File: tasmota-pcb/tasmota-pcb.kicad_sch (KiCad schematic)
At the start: 0 parts

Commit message: Add esp32 doit from https://gitlab.com/VictorLamoine/kicad
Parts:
- added U1: ESP32_DevKit_V1_DOIT, Doit:esp32_devkit_v1_doit, symbol Doit:ESP32_DevKit_V1_DOIT
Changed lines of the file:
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@@
 (kicad_sch (version 20230121) (generator eeschema)
   (paper "A4")
+  (symbol (lib_id "Doit:ESP32_DevKit_V1_DOIT") (at 124.46 91.44 0) (unit 1)
+    (in_bom yes) (on_board yes) (dnp no) (fields_autoplaced)
+    (property "Reference" "U1" (at 126.6541 53.34 0)
+      (effects (font (size 1.27 1.27)) (justify left))
+    )
+    (property "Value" "ESP32_DevKit_V1_DOIT" (at 126.6541 55.88 0)
+      (effects (font (size 1.27 1.27)) (justify left))
+    )
+    (property "Footprint" "Doit:esp32_devkit_v1_doit" (at 113.03 57.15 0)
+      (effects (font (size 1.27 1.27)) hide)
+    )
+    (property "Datasheet" "https://aliexpress.com/item/32864722159.html" (at 113.03 57.15 0)
+      (effects (font (size 1.27 1.27)) hide)
+    )
+    (pin "27")
+    (pin "30")
+    (pin "26")
+    (pin "22")
+    (pin "5")
+    (pin "15")
+    (pin "10")
+    (pin "16")
+    (pin "14")
+    (pin "6")
+    (pin "18")
+    (pin "21")
+    (pin "17")
+    (pin "19")
+    (pin "23")
+    (pin "28")
+    (pin "25")
+    (pin "4")
+    (pin "13")
+    (pin "3")
+    (pin "2")
+    (pin "20")
+    (pin "12")
+    (pin "11")
+    (pin "1")
+    (pin "24")
+    (pin "7")
+    (pin "9")
+    (pin "8")
+    (pin "29")
+    (instances
+      (project "tasmota-pcb"
+        (path "/0446fa3c-fa52-4d7b-8ba0-a6da357efbc3"
+          (reference "U1") (unit 1)
+        )
+      )
+    )
+  )
   (sheet_instances
     (path "/" (page "1"))

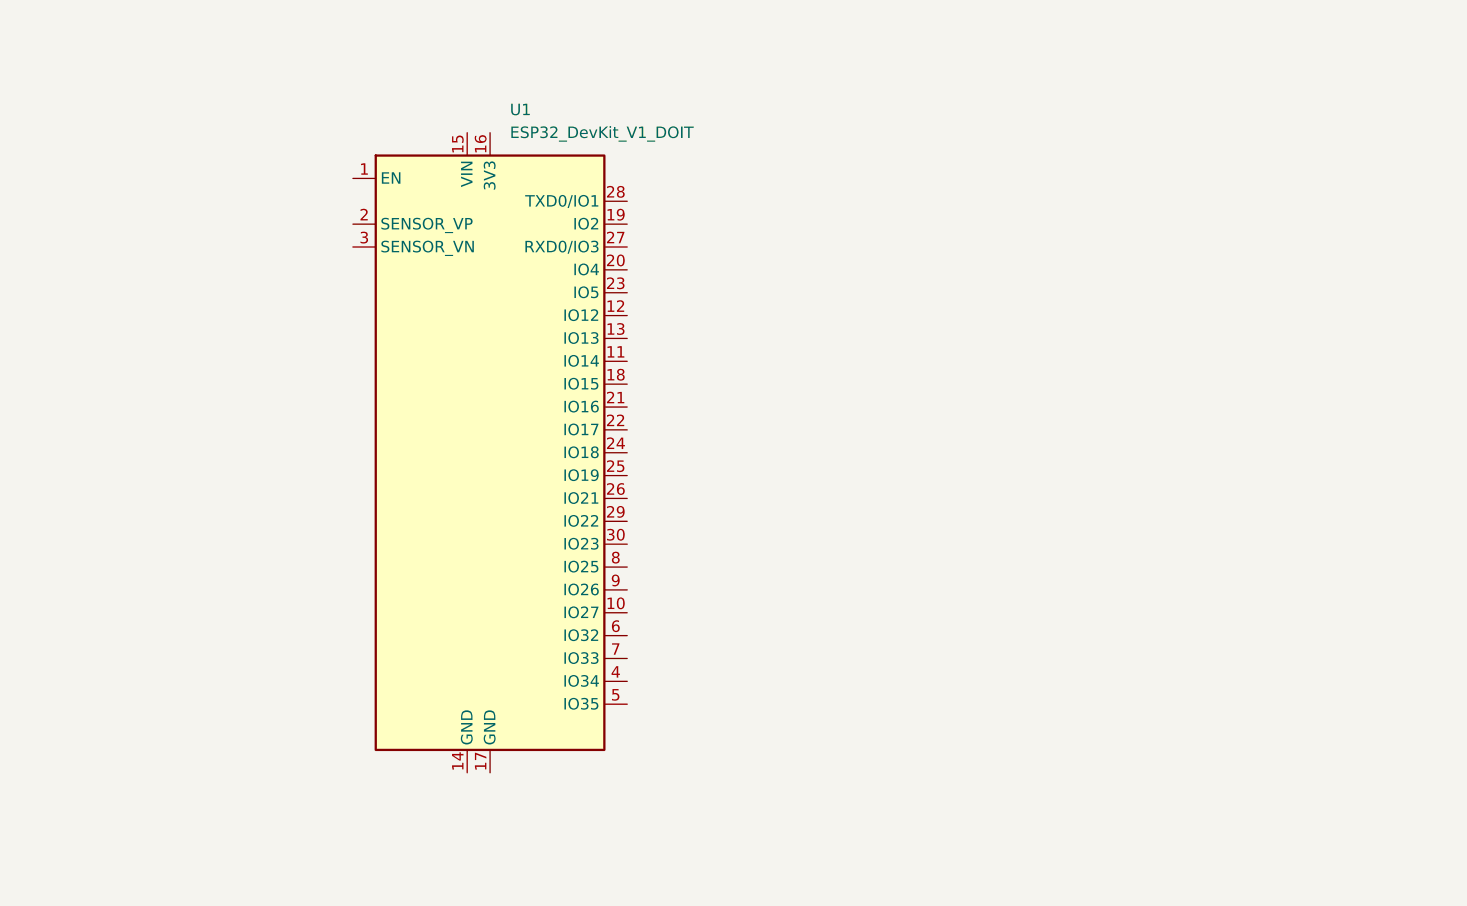
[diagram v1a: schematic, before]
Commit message: Add some IO and power
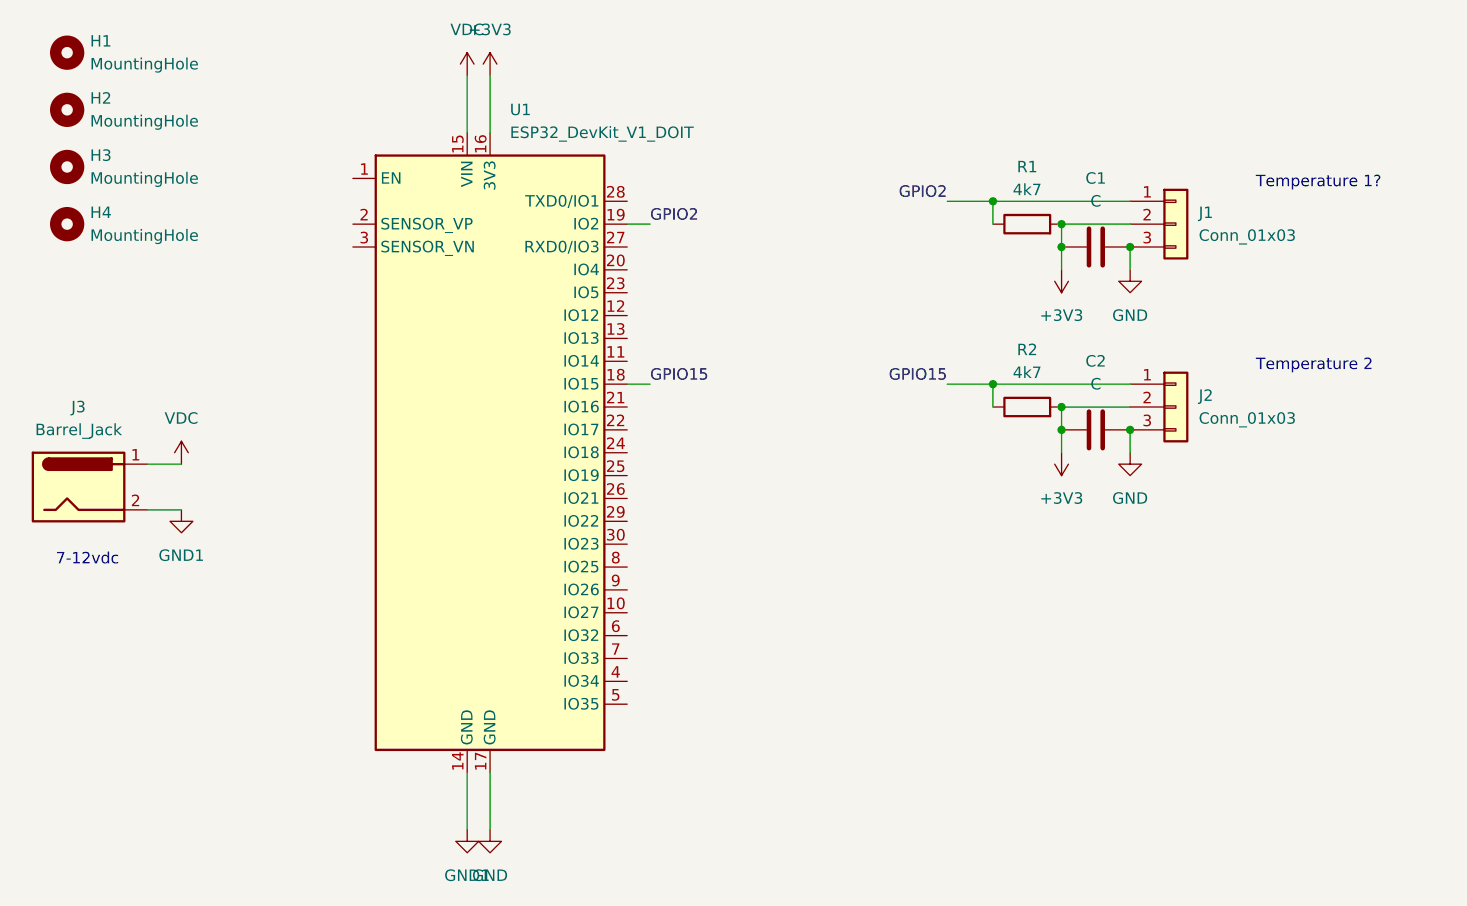
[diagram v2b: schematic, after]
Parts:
- added C1, C2: C, symbol Device:C
- added H1, H2, H3, H4: MountingHole, symbol Mechanical:MountingHole
- added J1, J2: Conn_01x03, symbol Connector_Generic:Conn_01x03
- added J3: Barrel_Jack, symbol Connector:Barrel_Jack
- added R1, R2: 4k7, symbol Device:R
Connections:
- net GND1: now reaches U1.14 (GND)
- net GND1: now also J3.2
- net VDC: now reaches U1.15 (VIN)
- net VDC: now also J3.1
- net +3V3: now reaches U1.16 (3V3)
- net +3V3: now also C1.1, C2.1, J1.2 (Pin_2), J2.2 (Pin_2), R1.2, R2.2
- net GND: now reaches U1.17 (GND)
- net GND: now also C1.2, C2.2, J1.3 (Pin_3), J2.3 (Pin_3)
- net GPIO15: now reaches U1.18 (IO15)
- net GPIO15: now also J2.1 (Pin_1), R2.1
- net GPIO2: now reaches U1.19 (IO2)
- net GPIO2: now also J1.1 (Pin_1), R1.1
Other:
- note added: "7-12vdc"
- note added: "Temperature 1?"
- note added: "Temperature 2"

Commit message: Layout pcb for case
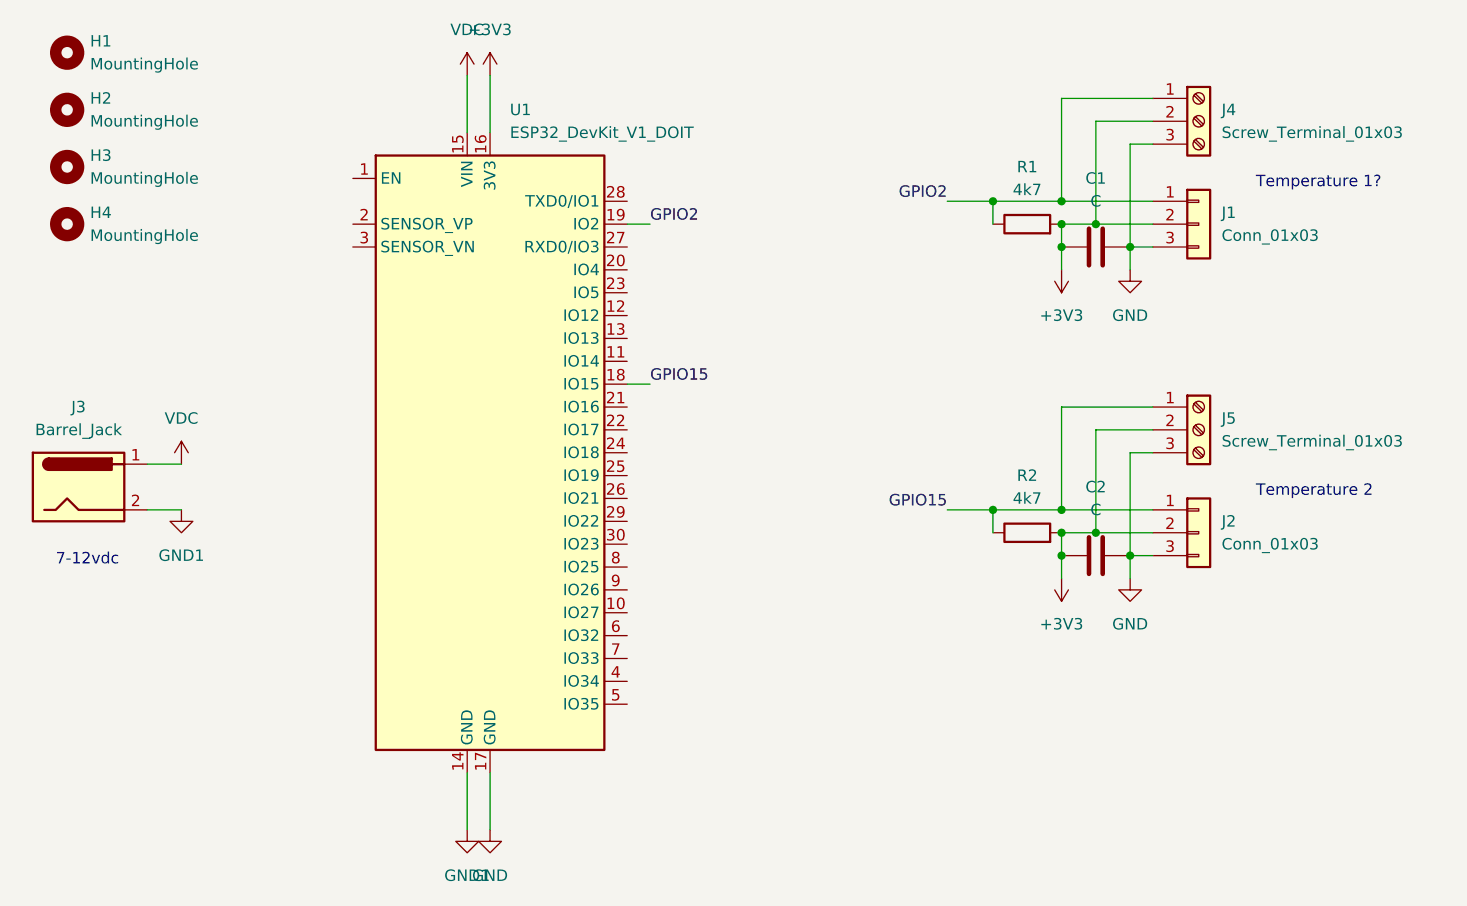
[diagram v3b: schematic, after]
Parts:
- added J4, J5: Screw_Terminal_01x03, TerminalBlock_Phoenix:TerminalBlock_Phoenix_MKDS-1,5-3_1x03_P5.00mm_Horizontal, symbol Connector:Screw_Terminal_01x03
- C1, C2: footprint (none) -> Capacitor_THT:CP_Radial_D4.0mm_P1.50mm
- H1, H2, H3, H4: footprint (none) -> MountingHole:MountingHole_6.4mm_M6
- J1, J2: footprint (none) -> Connector_PinHeader_2.54mm:PinHeader_1x03_P2.54mm_Horizontal
- J3: footprint (none) -> Connector_BarrelJack:BarrelJack_Wuerth_6941xx301002
- R1, R2: footprint (none) -> Resistor_THT:R_Axial_DIN0207_L6.3mm_D2.5mm_P10.16mm_Horizontal
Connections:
- net +3V3: now also J4.2 (Pin_2), J5.2 (Pin_2)
- net GND: now also J4.3 (Pin_3), J5.3 (Pin_3)
- net GPIO15: now also J5.1 (Pin_1)
- net GPIO2: now also J4.1 (Pin_1)
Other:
- moved on the sheet: C2, J1, J2, R2
